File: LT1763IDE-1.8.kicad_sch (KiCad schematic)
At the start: 6 parts, among them U3201 LT1763IDE-1.8#PBF

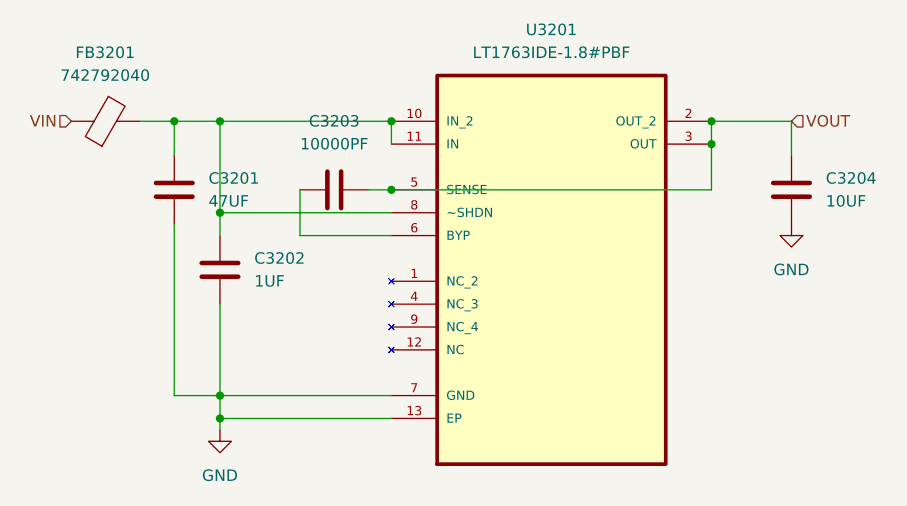
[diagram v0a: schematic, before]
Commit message: Updates from Michal to fix ERC errors
Still lots of ERC warnings
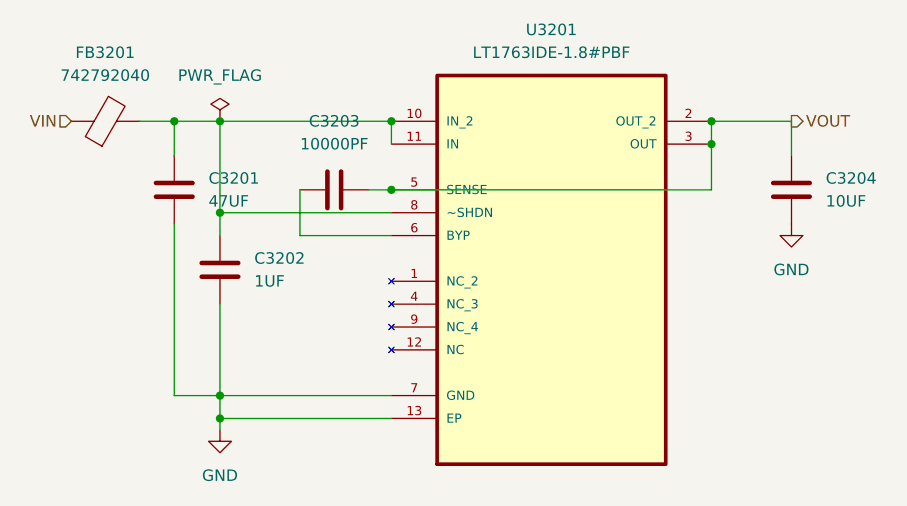
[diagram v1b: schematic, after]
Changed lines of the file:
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@@
 	)
 	(hierarchical_label "VOUT"
-		(shape input)
+		(shape output)
 		(at 180.34 74.93 0)
 		(fields_autoplaced yes)
@@
 					(unit 1)
 				)
+			)
+		)
+	)
+	(symbol
+		(lib_id "power:PWR_FLAG")
+		(at 116.84 74.93 0)
+		(unit 1)
+		(exclude_from_sim no)
+		(in_bom yes)
+		(on_board yes)
+		(dnp no)
+		(fields_autoplaced yes)
+		(property "Reference" "#FLG07"
+			(at 116.84 73.025 0)
+			(effects
+				(font
+					(size 1.27 1.27)
+				)
+				(hide yes)
+			)
+		)
+		(property "Value" "PWR_FLAG"
+			(at 116.84 69.85 0)
+			(effects
+				(font
+					(size 1.27 1.27)
+				)
+			)
+		)
+		(property "Footprint" ""
+			(at 116.84 74.93 0)
+			(effects
+				(font
+					(size 1.27 1.27)
+				)
+				(hide yes)
+			)
+		)
+		(property "Datasheet" "~"
+			(at 116.84 74.93 0)
+			(effects
+				(font
+					(size 1.27 1.27)
+				)
+				(hide yes)
+			)
+		)
+		(property "Description" "Special symbol for telling ERC where power comes from"
+			(at 116.84 74.93 0)
+			(effects
+				(font
+					(size 1.27 1.27)
+				)
+				(hide yes)
+			)
+		)
+		(pin "1"
+		)
+		(instances
+			(project "zest"
+				(path "/00000000-0000-0000-0000-000000000003/00000000-0000-0000-0000-000000000002/0c35330d-b251-450f-a1ea-5c811d7f51a9"
+					(reference "#FLG07")
+					(unit 1)
+				)

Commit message: Schematic Changes
Added Manufacturer/MPN/Description Fields to parts
Added libraries to project
Modified FMC schematic to use new symbol
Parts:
- C3201: Manufacturer (none) -> Murata; Manufacturer Part Number (none) -> GRM31CR61A476ME15L
- C3202: Manufacturer (none) -> Murata; Manufacturer Part Number (none) -> GRM188R61E105KA12D
- C3203: Manufacturer (none) -> TDK; Manufacturer Part Number (none) -> C1608C0G1E103J080AA
- C3204: Manufacturer (none) -> TDK; Manufacturer Part Number (none) -> C1608X5R1A106M080AC
- FB3201: Manufacturer (none) -> Würth; Manufacturer Part Number (none) -> 742792040
- U3201: Manufacturer (none) -> Analog Devices; Manufacturer Part Number (none) -> LT1763IDE-1.8#PBF
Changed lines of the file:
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@@
 			)
 		)
-		(property "Description" "Ferrite bead"
+		(property "Description" "FERRITE BEAD 600 OHM 0805 1LN"
 			(at 104.14 74.93 0)
 			(effects
@@
 		(property "Vendor" "digikey:732-1620-1-ND"
 			(at 179.07 179.07 0)
+			(effects
+				(font
+					(size 1.27 1.27)
+				)
+				(hide yes)
+			)
+		)
+		(property "Manufacturer" "Würth"
+			(at 104.14 74.93 0)
+			(effects
+				(font
+					(size 1.27 1.27)
+				)
+				(hide yes)
+			)
+		)
+		(property "Manufacturer Part Number" "742792040"
+			(at 104.14 74.93 0)
 			(effects
 				(font
@@
 			)
 		)
-		(property "Description" ""
+		(property "Description" "IC REG LINEAR 1.8V 500MA 12DFN"
 			(at 153.67 87.63 0)
 			(effects
@@
 		(property "Vendor" "digikey:LT1763IDE-1.8#PBF-ND"
 			(at 0 175.26 0)
+			(effects
+				(font
+					(size 1.27 1.27)
+				)
+				(hide yes)
+			)
+		)
+		(property "Manufacturer" "Analog Devices"
+			(at 153.67 87.63 0)
+			(effects
+				(font
+					(size 1.27 1.27)
+				)
+				(hide yes)
+			)
+		)
+		(property "Manufacturer Part Number" "LT1763IDE-1.8#PBF "
+			(at 153.67 87.63 0)
 			(effects
 				(font
@@
 			)
 		)
-		(property "Description" "Unpolarized capacitor"
+		(property "Description" "CAP CER 47UF 10V X5R 1206"
 			(at 111.76 82.55 0)
 			(effects
@@
 		(property "Vendor" "digikey:490-5528-1-ND"
 			(at 223.52 0 0)
+			(effects
+				(font
+					(size 1.27 1.27)
+				)
+				(hide yes)
+			)
+		)
+		(property "Manufacturer" "Murata"
+			(at 111.76 82.55 0)
+			(effects
+				(font
+					(size 1.27 1.27)
+				)
+				(hide yes)
+			)
+		)
+		(property "Manufacturer Part Number" "GRM31CR61A476ME15L "
+			(at 111.76 82.55 0)
 			(effects
 				(font
@@
 			)
 		)
-		(property "Description" "Unpolarized capacitor"
+		(property "Description" "CAP CER 10UF 10V X5R 0603"
 			(at 180.34 82.55 0)
 			(effects
@@
 		(property "Vendor" "digikey:445-6853-1-ND"
 			(at 0 165.1 0)
+			(effects
+				(font
+					(size 1.27 1.27)
+				)
+				(hide yes)
+			)
+		)
+		(property "Manufacturer" "TDK"
+			(at 180.34 82.55 0)
+			(effects
+				(font
+					(size 1.27 1.27)
+				)
+				(hide yes)
+			)
+		)
+		(property "Manufacturer Part Number" "C1608X5R1A106M080AC"
+			(at 180.34 82.55 0)
 			(effects
 				(font
@@
 			)
 		)
-		(property "Description" "Unpolarized capacitor"
+		(property "Description" "CAP CER 1UF 25V X5R 0603"
 			(at 116.84 91.44 0)
 			(effects
@@
 		(property "Vendor" "digikey:490-3897-1-ND"
 			(at 233.68 0 0)
+			(effects
+				(font
+					(size 1.27 1.27)
+				)
+				(hide yes)
+			)
+		)
+		(property "Manufacturer" "Murata"
+			(at 116.84 91.44 0)
+			(effects
+				(font
+					(size 1.27 1.27)
+				)
+				(hide yes)
+			)
+		)
+		(property "Manufacturer Part Number" "GRM188R61E105KA12D"
+			(at 116.84 91.44 0)
 			(effects
 				(font
@@
 			)
 		)
-		(property "Description" "Unpolarized capacitor"
+		(property "Description" "CAP CER 10000PF 25V C0G 0603"
 			(at 129.54 82.55 0)
 			(effects
@@
 			(effects
 				(font
+					(size 1.27 1.27)
+				)
+				(hide yes)
+			)
+		)
+		(property "Manufacturer" "TDK"
+			(at 129.54 82.55 0)
+			(effects
+				(font
+					(size 1.27 1.27)
+				)
+				(hide yes)
+			)
+		)
+		(property "Manufacturer Part Number" "C1608C0G1E103J080AA"
+			(at 129.54 82.55 0)
+			(effects
+				(font

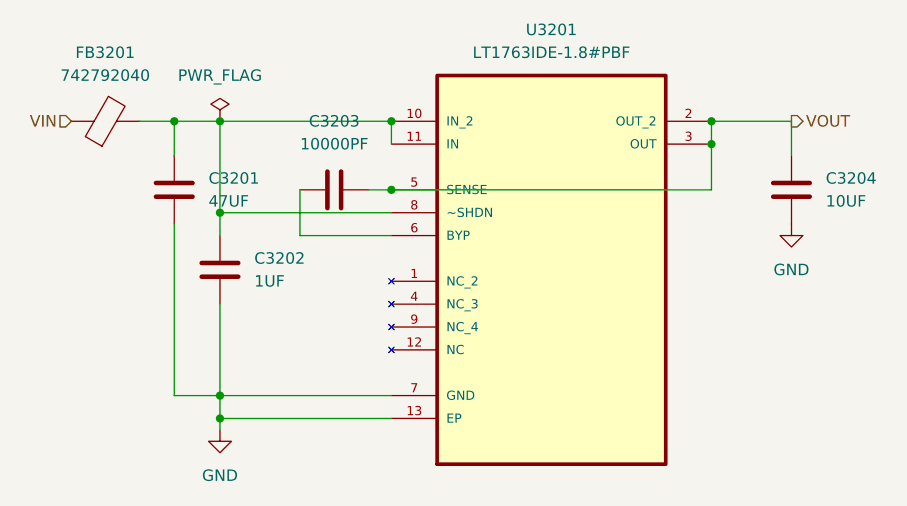
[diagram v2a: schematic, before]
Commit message: Schematics update
Cleaned up RF ADC and front end sections.
Verified that changes did not changes anything about the layout.
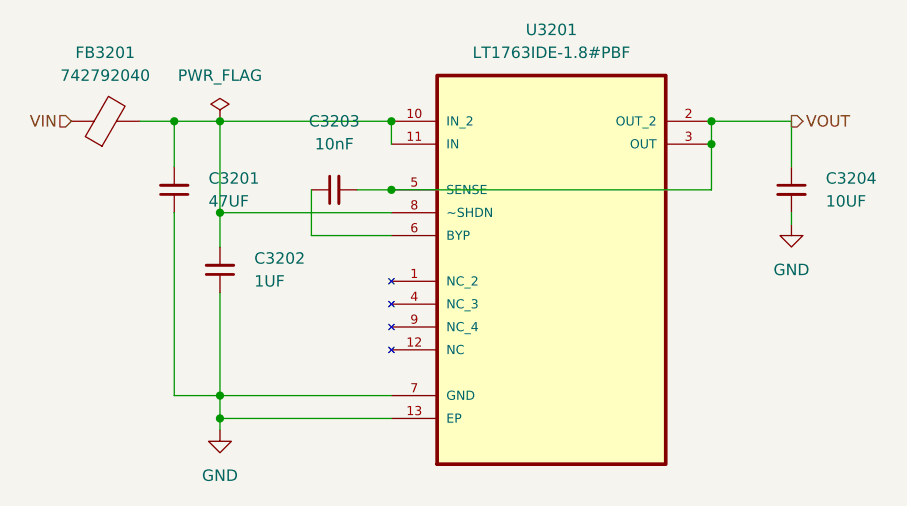
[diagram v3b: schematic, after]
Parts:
- C3201, C3202, C3204: symbol Device:C -> Device:C_Small
- C3203: value 10000PF -> 10nF; symbol Device:C -> Device:C_Small
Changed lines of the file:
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@@
 	(wire
 		(pts
-			(xy 116.84 105.41) (xy 116.84 95.25)
+			(xy 116.84 105.41) (xy 116.84 93.98)
 		)
 		(stroke
@@
 	(wire
 		(pts
-			(xy 116.84 85.09) (xy 116.84 87.63)
+			(xy 116.84 85.09) (xy 116.84 88.9)
 		)
 		(stroke
@@
 	(wire
 		(pts
-			(xy 125.73 82.55) (xy 125.73 87.63)
-		)
-		(stroke
-			(width 0)
-			(type default)
-		)
-	)
-	(wire
-		(pts
-			(xy 111.76 86.36) (xy 111.76 105.41)
+			(xy 127 82.55) (xy 127 87.63)
+		)
+		(stroke
+			(width 0)
+			(type default)
+		)
+	)
+	(wire
+		(pts
+			(xy 111.76 85.09) (xy 111.76 105.41)
 		)
 		(stroke
@@
 	(wire
 		(pts
-			(xy 125.73 87.63) (xy 135.89 87.63)
-		)
-		(stroke
-			(width 0)
-			(type default)
-		)
-	)
-	(wire
-		(pts
-			(xy 180.34 74.93) (xy 180.34 78.74)
+			(xy 127 87.63) (xy 135.89 87.63)
+		)
+		(stroke
+			(width 0)
+			(type default)
+		)
+	)
+	(wire
+		(pts
+			(xy 180.34 74.93) (xy 180.34 80.01)
 		)
 		(stroke
@@
 	(wire
 		(pts
-			(xy 133.35 82.55) (xy 135.89 82.55)
-		)
-		(stroke
-			(width 0)
-			(type default)
-		)
-	)
-	(wire
-		(pts
-			(xy 111.76 78.74) (xy 111.76 74.93)
+			(xy 132.08 82.55) (xy 135.89 82.55)
+		)
+		(stroke
+			(width 0)
+			(type default)
+		)
+	)
+	(wire
+		(pts
+			(xy 111.76 80.01) (xy 111.76 74.93)
 		)
 		(stroke
@@
 		(pts
 			(xy 111.76 105.41) (xy 116.84 105.41)
+		)
+		(stroke
+			(width 0)
+			(type default)
+		)
+	)
+	(wire
+		(pts
+			(xy 180.34 85.09) (xy 180.34 86.36)
 		)
 		(stroke
@@
 	)
 	(symbol
-		(lib_id "Device:C")
+		(lib_id "Device:C_Small")
 		(at 111.76 82.55 180)
 		(unit 1)
@@
 	)
 	(symbol
-		(lib_id "Device:C")
+		(lib_id "Device:C_Small")
 		(at 180.34 82.55 0)
 		(unit 1)
@@
 	)
 	(symbol
-		(lib_id "Device:C")
+		(lib_id "Device:C_Small")
 		(at 116.84 91.44 180)
 		(unit 1)
@@
 	)
 	(symbol
-		(lib_id "Device:C")
+		(lib_id "Device:C_Small")
 		(at 129.54 82.55 90)
 		(unit 1)
@@
 			)
 		)
-		(property "Value" "10000PF"
+		(property "Value" "10nF"
 			(at 129.54 77.47 90)
 			(effects
@@
 			)
 		)
-		(property "Description" "CAP CER 10000PF 25V C0G 0603"
+		(property "Description" "CAP CER 10nF 25V C0G 0603"
 			(at 129.54 82.55 0)
 			(effects
